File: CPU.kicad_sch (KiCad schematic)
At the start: 13 parts

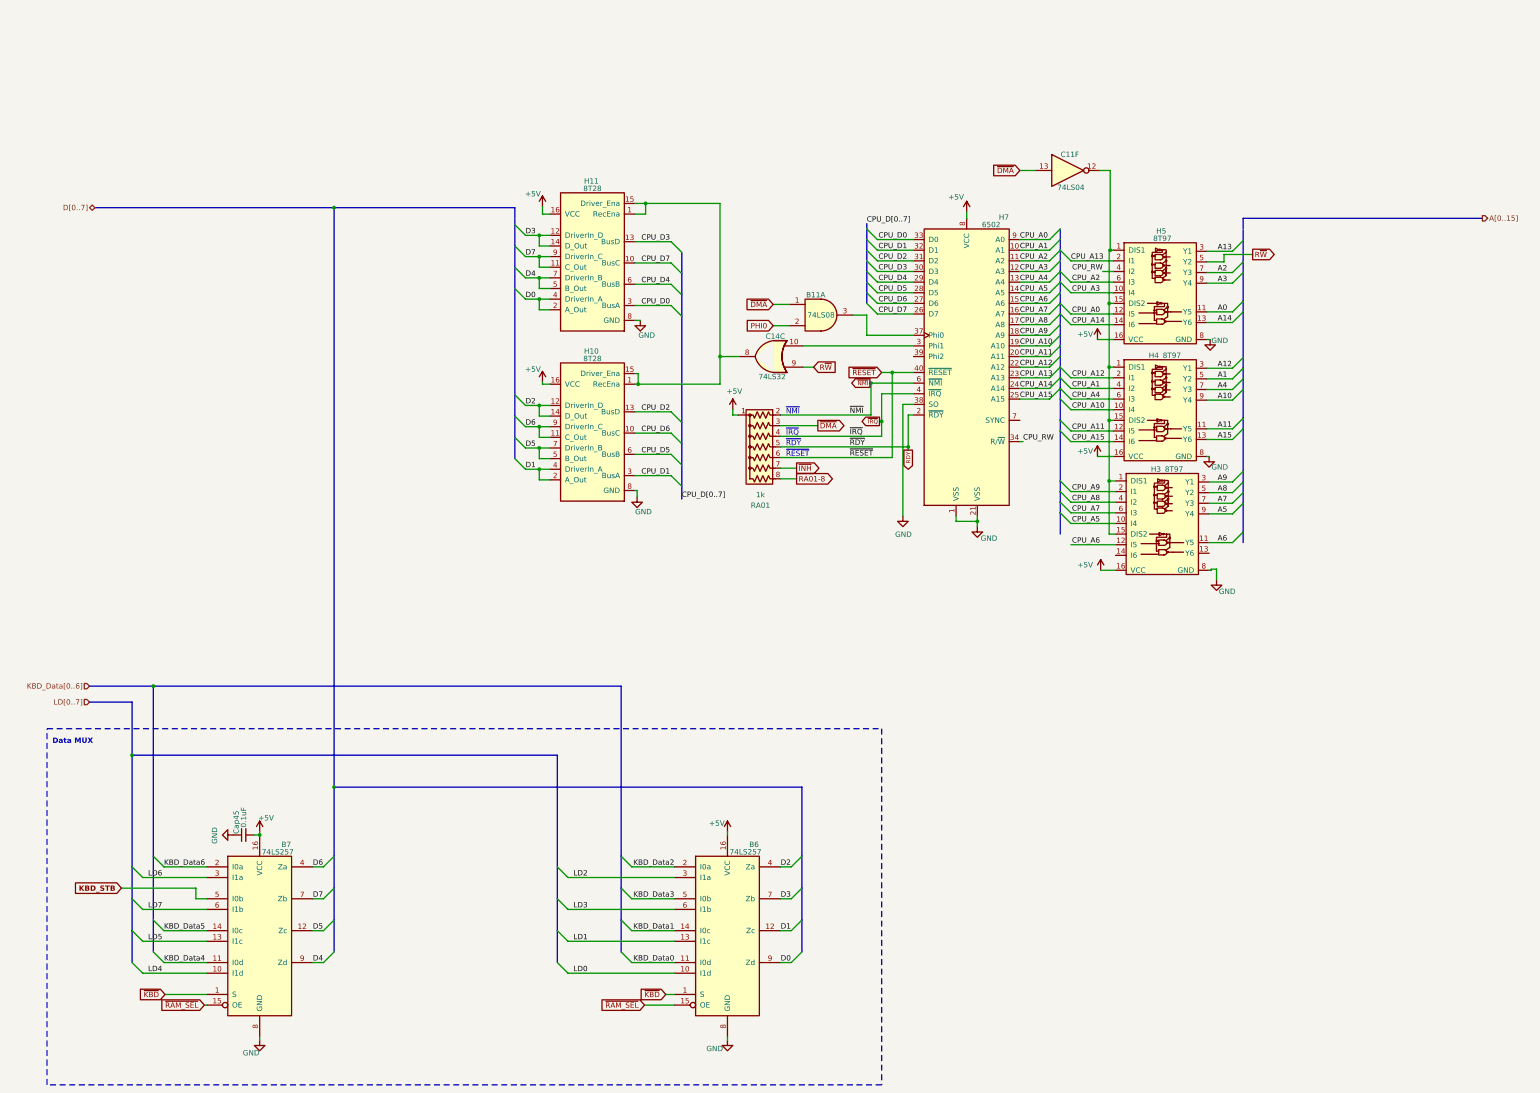
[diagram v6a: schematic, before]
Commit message: add missing test points
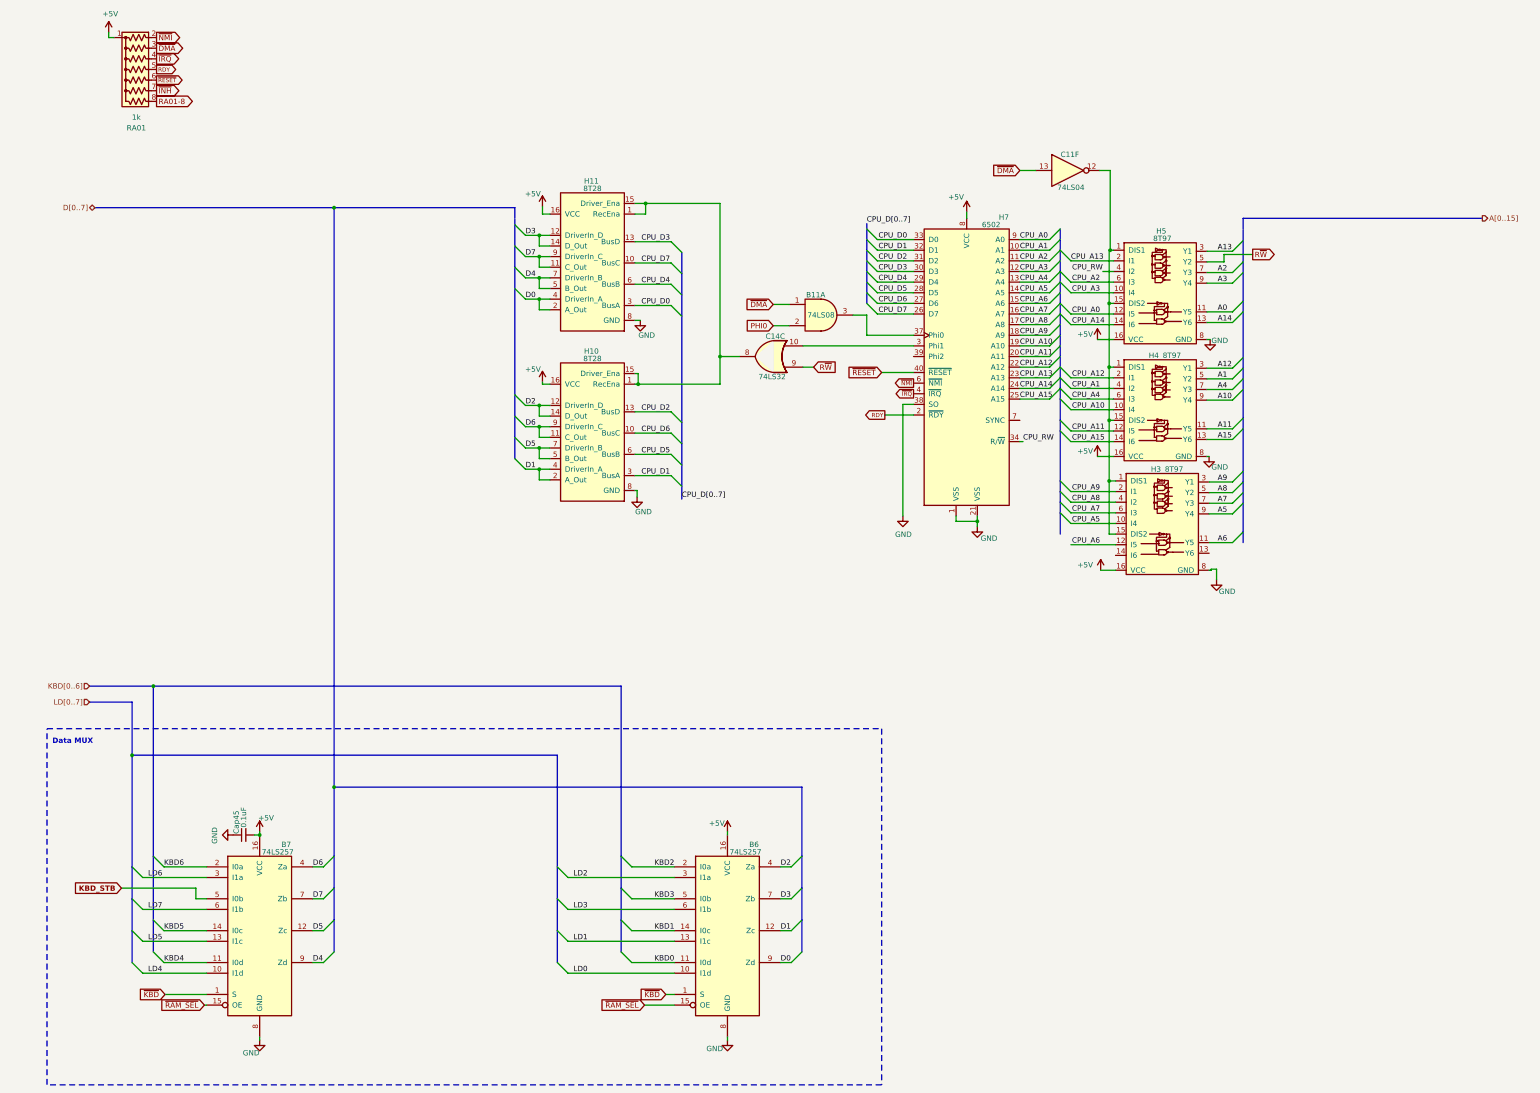
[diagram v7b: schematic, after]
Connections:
- net KBD_Data0 renamed KBD0
- net KBD_Data1 renamed KBD1
- net KBD_Data2 renamed KBD2
- net KBD_Data3 renamed KBD3
- net KBD_Data4 renamed KBD4
- net KBD_Data5 renamed KBD5
- net KBD_Data6 renamed KBD6
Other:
- note removed: "~{IRQ}"
- note removed: "~{NMI}"
- note removed: "~{RDY}"
- note removed: "~{RESET}"
